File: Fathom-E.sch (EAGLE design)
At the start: 6 parts

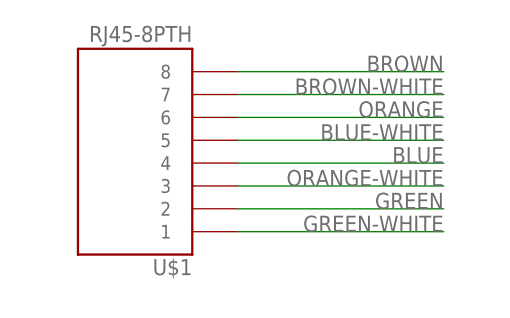
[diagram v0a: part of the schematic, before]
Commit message: Updated RJ45 position on Fathom-E
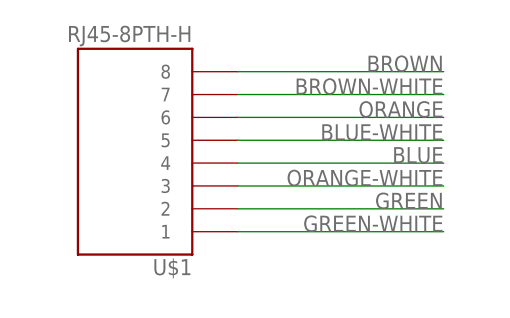
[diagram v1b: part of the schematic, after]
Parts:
- U$1: value RJ45-8PTH -> RJ45-8PTH-H; device SparkFun-Connectors:RJ45-8PTH -> BlueRobotics-Main:RJ45-8PTH-H
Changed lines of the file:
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@@
 <part name="U$6" library="BlueRobotics-Main" deviceset="LOGO" device="BR-LOGO-MS-COPPER"/>
 <part name="U$7" library="BlueRobotics-Main" deviceset="LOGO" device="FULL-M"/>
-<part name="U$1" library="SparkFun-Connectors" deviceset="RJ45-8" device="PTH"/>
+<part name="U$1" library="BlueRobotics-Main" deviceset="RJ45-8" device="PTH-H"/>
 <part name="JP1" library="SparkFun-Connectors" deviceset="M08" device="3.5MM-8"/>
 </parts>
